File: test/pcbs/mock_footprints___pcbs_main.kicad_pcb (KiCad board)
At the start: 2 copper layers, 39 x 19 mm, 7 parts

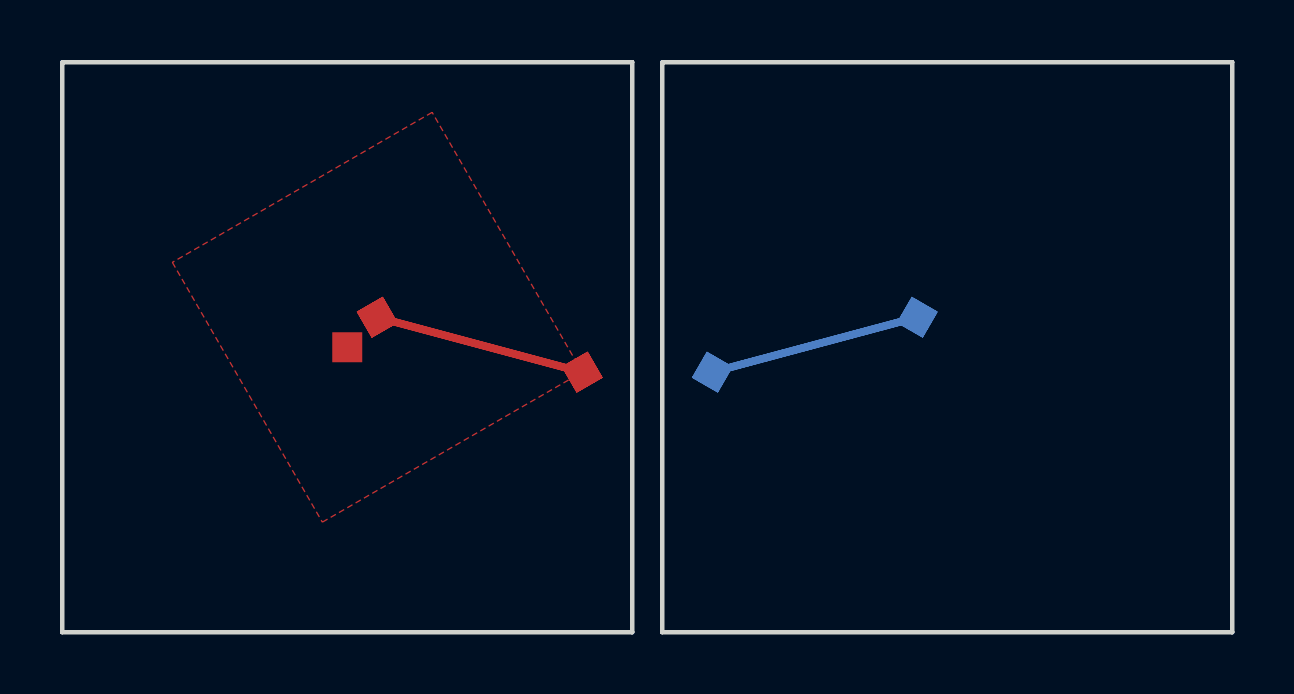
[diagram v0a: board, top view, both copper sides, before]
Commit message: Expand test coverage (#77)
* ignore line endings in cli tests
* ignore line endings in integration tests
* expand code coverage for `choc` footprint
* expand code coverage for `chocmini` footprint
* expand code coverage for `mx` footprint
* expand code coverage for `pad` footprint
* expand code coverage for rest of footprints
* expand code coverage for `anchor.js`
* expand code coverage for `units.js`
* expand code coverage for `points.js`
* expand code coverage for `filter.js`
* expand code coverage for `outlines.js`
* expand code coverage for `pcbs.js`
* expand code coverage for `ergogen.js`
* expand code coverage for `kle.js`
* more code coverage for `outlines.js`
* expand code coverage for `cases.js`
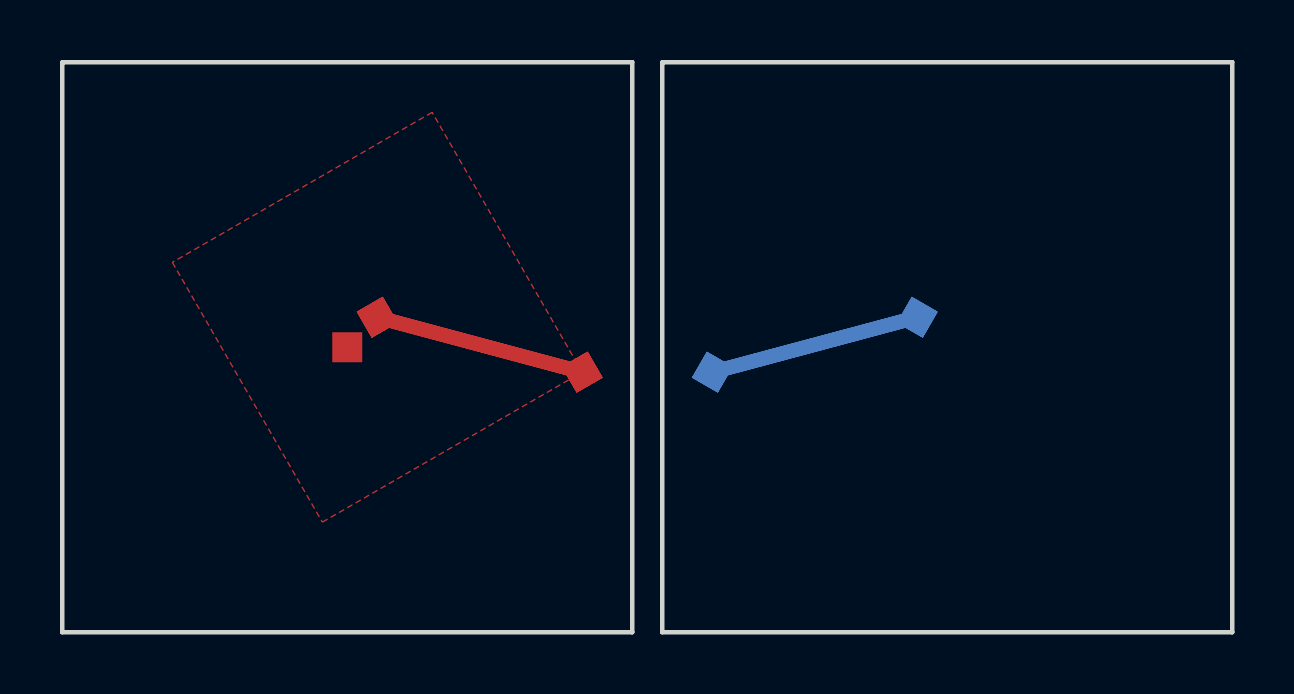
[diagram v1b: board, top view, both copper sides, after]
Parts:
- removed the ? at (1.00, -1.00) (x2)
- removed the ? at (19.0, -1.00) (x2)
- removed the ? at (0.00, 0.00)
- added ? (x2): , trace_test, F.Cu at (1.00, -1.00)
- added ? (x2): , trace_test, B.Cu at (19.0, -1.00)
- added ? (x2): , anchor_test, F.Cu at (0.00, 0.00)
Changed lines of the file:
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@@
                         (net 1 "P1") (solder_mask_margin 0.2))
                 )
-                (segment (start 1 -1) (end 7.830127 0.8301270000000001) (width 0.25) (layer F.Cu) (net 1))
+                (segment (start 1 -1) (end 7.830127 0.8301270000000001) (width 0.475) (layer F.Cu) (net 1))
                 (module trace_test (layer B.Cu)
                     (at 19 -1 -30)
@@
                         (net 1 "P1") (solder_mask_margin 0.2))
                 )
-                (segment (start 19 -1) (end 12.169872999999999 0.8301270000000001) (width 0.25) (layer B.Cu) (net 1))
+                (segment (start 19 -1) (end 12.169872999999999 0.8301270000000001) (width 0.475) (layer B.Cu) (net 1))
                 (module trace_test (layer B.Cu)
                     (at 19 -1 -30)
@@
                         (net 1 "P1") (solder_mask_margin 0.2))
                 )
-                (segment (start 19 -1) (end 12.169872999999999 0.8301270000000001) (width 0.25) (layer B.Cu) (net 1))
+                (segment (start 19 -1) (end 12.169872999999999 0.8301270000000001) (width 0.475) (layer B.Cu) (net 1))
                 (module trace_test (layer F.Cu)
                     (at 1 -1 30)
@@
                         (net 1 "P1") (solder_mask_margin 0.2))
                 )
-                (segment (start 1 -1) (end 7.830127 0.8301270000000001) (width 0.25) (layer F.Cu) (net 1))
+                (segment (start 1 -1) (end 7.830127 0.8301270000000001) (width 0.475) (layer F.Cu) (net 1))
                 (module zone_test (layer F.Cu)
                     (at 1 -1 30)
@@
                     (fp_line (start 0 0) (end 10 -10) (layer Dwgs.User) (width 0.05))
                 )
+                (module anchor_test (layer F.Cu)
+                    (at 0 0 0)
+                    (fp_line (start 0 0) (end 0 0) (layer Dwgs.User) (width 0.05))
+                )
             (gr_line (start -9.5 9.5) (end 9.5 9.5) (angle 90) (layer Edge.Cuts) (width 0.15))

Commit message: Getting coverage to 100%
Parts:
- removed the ? at (1.00, -1.00) (x2)
- removed the ? at (19.0, -1.00) (x2)
- removed the ? at (0.00, 0.00) (x2)
- added ? (x2): , trace_test, F.Cu at (1.00, -1.00)
- added ? (x2): , trace_test, B.Cu at (19.0, -1.00)
- added ? (x2): , anchor_test, F.Cu at (0.00, 0.00)
- added ?: , arrobj_test, F.Cu at (0.00, 0.00)
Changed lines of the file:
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@@
                     (fp_line (start 0 0) (end 0 0) (layer Dwgs.User) (width 0.05))
+                )
+                (module arrobj_test (layer F.Cu)
+                    (at 0 0 0)
+                    (fp_line (start 5 5) (end 6 6) (layer Dwgs.User) (width 0.05))
+(fp_line (start 5 5) (end 7 7) (layer Dwgs.User) (width 0.05))
                 )
             (gr_line (start -9.5 9.5) (end 9.5 9.5) (angle 90) (layer Edge.Cuts) (width 0.15))
